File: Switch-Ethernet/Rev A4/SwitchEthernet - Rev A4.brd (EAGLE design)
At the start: 86 x 90 mm, 118 parts, among them J1 22-05-7028-02, J2 DF17(2.0)-20DP-0.5V(57), J3 DF17(4.0)-20DP-0.5V(57), J4 22-05-7058-05, P1 RB1-125BAG1A, T1 H1102FNL, T2 H1102FNL, U1 TC1264-3.3, U2 TC1264-1.8, U3 KSZ8995MA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

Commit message: Route the board
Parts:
- removed LED2, LED3: Green, led:CHIP-LED0603
- removed R1, R2: 1k5, rcl:R0603
- removed TP1, TP3, TP5: TPB1,27, testpad:B1,27
- moved CR1 123.8 mm to (16.5, 61.3), turned to 90 degrees
- moved C19 123.2 mm to (12.4, 60.6), turned to 90 degrees
- moved C20 122.3 mm to (13.0, 48.6), turned to 180 degrees
- moved C21 121.8 mm to (13.0, 46.7), turned to 180 degrees
- moved L3 120.3 mm to (16.5, 54.0), turned to 270 degrees
- moved C18 119.7 mm to (14.0, 60.6), turned to 90 degrees
- moved C4 109.3 mm to (19.7, 60.6), turned to 90 degrees
- moved R27 109.0 mm to (3.17, 58.4), turned to 180 degrees
- moved LED1 107.5 mm to (3.17, 60.3), turned to 90 degrees
- moved C1 106.9 mm to (18.7, 46.4), turned to 270 degrees
- moved U1 101.1 mm to (23.2, 50.2), turned to 90 degrees
- moved U2 101.1 mm to (24.4, 59.1), turned to 90 degrees
- moved C2 96.1 mm to (27.6, 49.8), turned to 90 degrees
- moved C3 94.3 mm to (28.3, 59.1), turned to 90 degrees
- moved C45 54.1 mm to (71.8, 69.5), flipped to the bottom, turned to 270 degrees
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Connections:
- removed net N$2: LED2.A, R1.1
- removed net N$6: LED3.A, R2.1
- net +1V8: no longer R1.2, TP1.TP
- net +3V3: no longer R2.2, TP5.TP
- net +5V: no longer TP3.TP
- net GND: no longer LED2.C, LED3.C
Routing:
- net +3V3: track 19.4 -> 50.1 mm, vias 8 -> 25
- net +1V8: track 0.00 -> 30.1 mm, vias 0 -> 11
- net RST_N: track 2.36 -> 17.6 mm
- net SDA: track 21.7 -> 26.2 mm
- net SCL_EEPROM: track 0.00 -> 3.27 mm
- net SDA_EEPROM: track 0.00 -> 3.14 mm
- net SCL: track 18.2 -> 21.2 mm
- net CT_2: track 49.0 -> 51.1 mm
- net RX1_ISO_N: track 32.4 -> 33.3 mm
- net X1: track 7.57 -> 8.52 mm
- net X2: track 6.21 -> 7.17 mm
- net RX1_ISO_P: track 30.6 -> 31.3 mm
- net TX3_ISO_P: track 56.3 -> 56.9 mm
- net TX3_ISO_N: track 52.4 -> 53.1 mm
- added copper zone on layer 1, net +1V8
- added copper zone on layer 15, net +1V8
- added copper zone on layer 1, net +3V3
- added copper zone on layer 1, net +5V
- added copper zone on layer 1, net PW

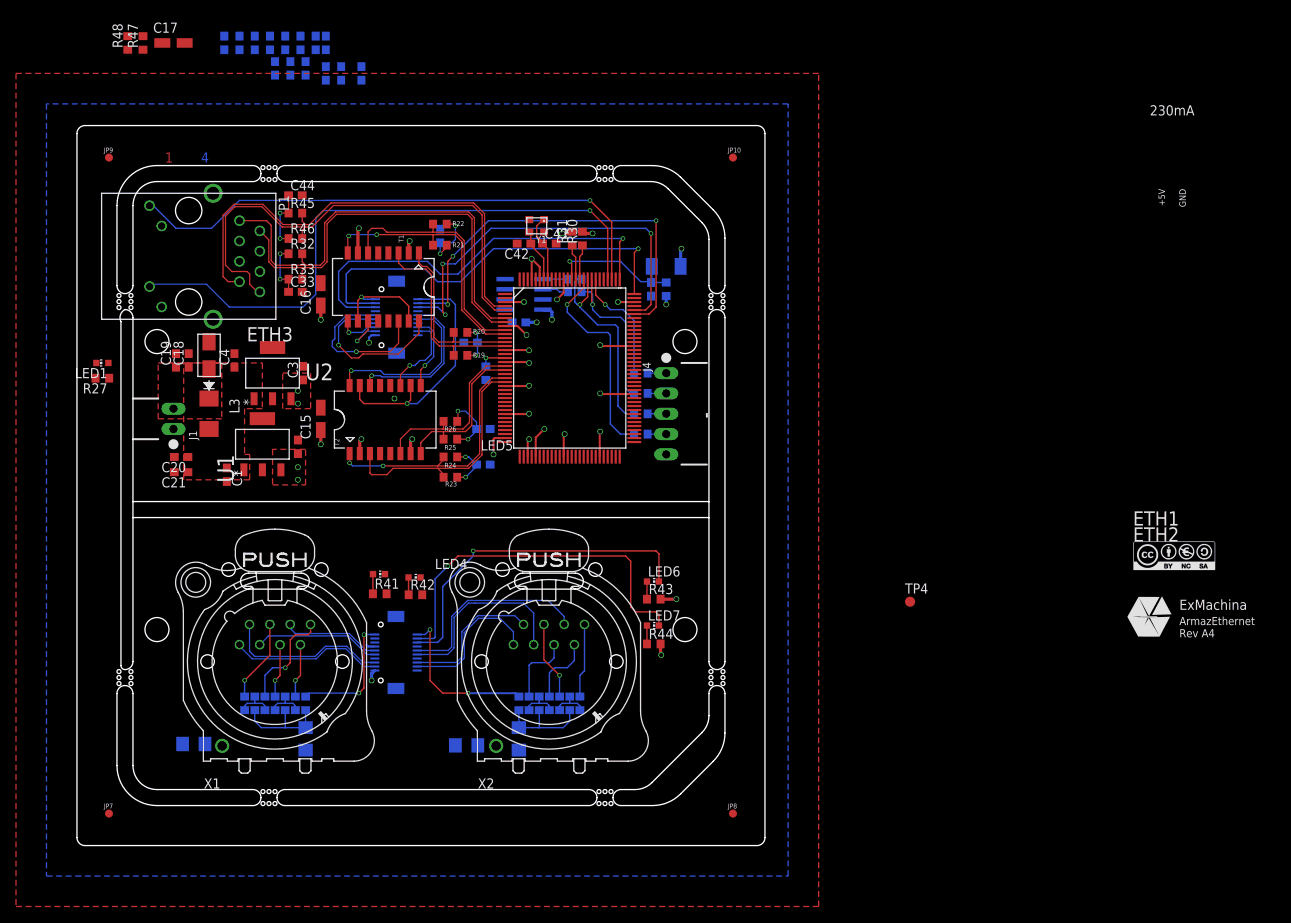
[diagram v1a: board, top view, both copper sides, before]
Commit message: Route LED +5V
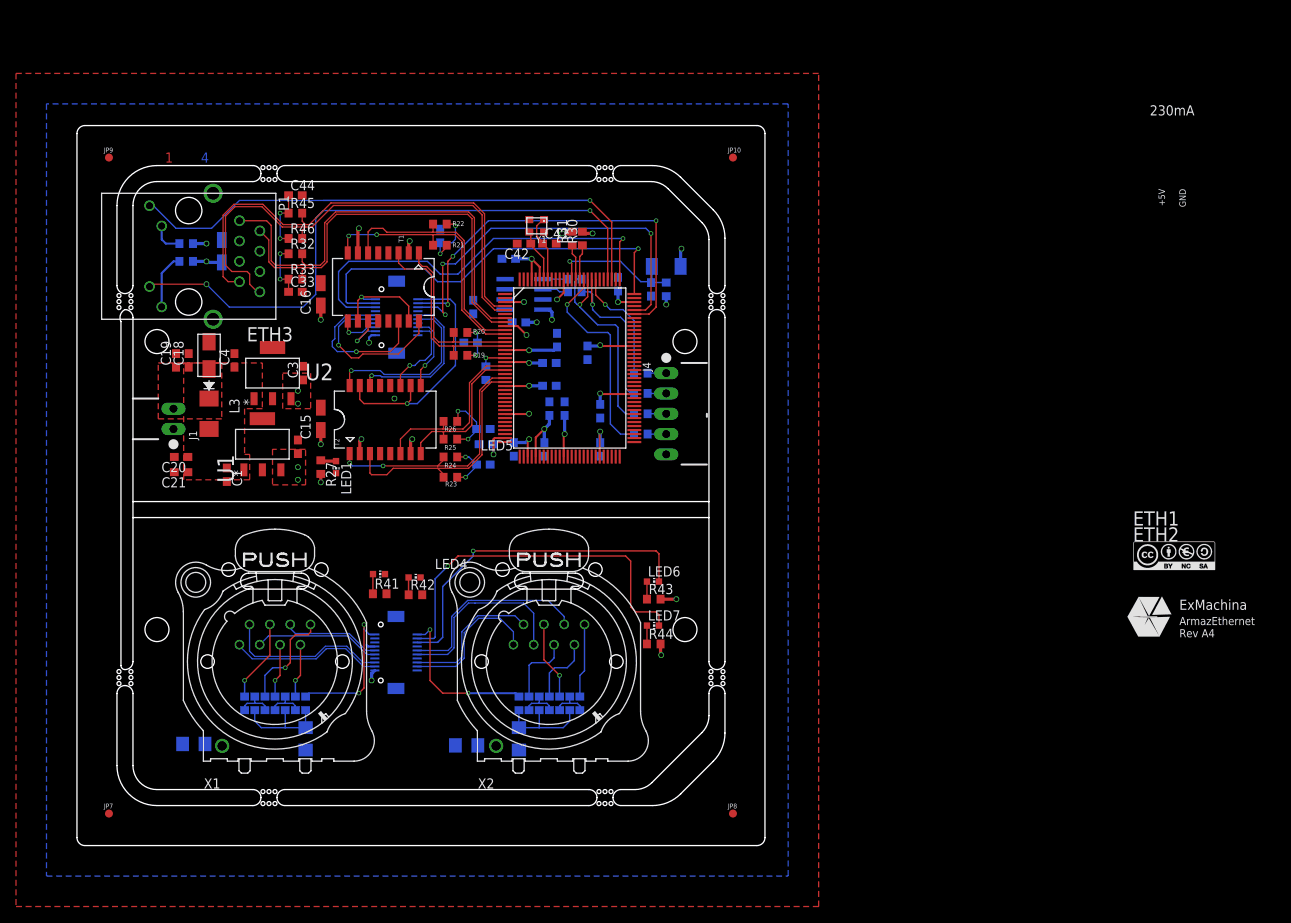
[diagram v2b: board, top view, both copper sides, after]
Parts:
- removed TP4: TPB1,27, testpad:B1,27
- moved C38 62.4 mm to (54.6, 49.5), turned to 270 degrees
- moved C37 60.2 mm to (58.4, 49.5), turned to 270 degrees
- moved C34 58.7 mm to (61.0, 54.6)
- moved C36 58.7 mm to (59.1, 54.6)
- moved C32 55.7 mm to (65.4, 49.5)
- moved C28 53.2 mm to (65.4, 54.3)
- moved C30 53.0 mm to (51.1, 50.2), turned to 0 degrees
- moved C31 50.7 mm to (63.8, 61.6), turned to 270 degrees
- moved C29 50.7 mm to (67.6, 70.2), turned to 90 degrees
- moved C27 48.0 mm to (59.1, 57.5), turned to 180 degrees
- moved C40 47.9 mm to (60.0, 63.2)
- moved C26 47.8 mm to (59.1, 60.3), turned to 180 degrees
- moved C35 43.1 mm to (54.0, 73.3), turned to 0 degrees
- moved C39 39.5 mm to (49.5, 67.3), turned to 270 degrees
- moved LED1 32.0 mm to (32.4, 47.3), turned to 180 degrees
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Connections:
- net GND: no longer TP4.TP
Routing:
- net +1V8: track 30.1 -> 45.5 mm
- net +3V3: track 50.1 -> 64.3 mm, vias 25 -> 28
- net N$35: track 0.00 -> 7.04 mm
- net N$34: track 0.00 -> 4.10 mm
- net CT_1: track 29.1 -> 31.2 mm
- net N$23: track 0.00 -> 1.95 mm
- net +5V: track 0.00 -> 1.05 mm
- net L3-1: vias 1 -> 2

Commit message: Finish the routing
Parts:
- moved LED1 20.7 mm to (11.7, 46.4), turned to 90 degrees
- moved R27 15.3 mm to (15.2, 46.4), turned to 0 degrees
- moved LED5 5.48 mm to (38.0, 30.0), turned to 90 degrees
- moved R41 5.44 mm to (41.5, 35.5)
- moved LED6 2.50 mm to (72.0, 35.5)
- moved LED7 2.50 mm to (72.0, 30.0)
- moved R44 2.50 mm to (72.1, 27.7)
- moved R43 2.50 mm to (72.1, 33.3)
- moved C21 1.59 mm to (14.0, 47.9)
- moved C20 1.59 mm to (14.0, 49.8)
- moved LED4 1.58 mm to (38.0, 35.5), turned to 90 degrees
- moved R42 1.57 mm to (41.5, 30.0)
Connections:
- net GND: no longer J2.11, J2.14, J2.17, J2.4, J2.7, J3.11, J3.14, J3.17, J3.4, J3.7
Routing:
- net L1-1: track 52.4 -> 66.5 mm, vias 1 -> 2
- net L1-2: track 52.2 -> 59.4 mm, vias 1 -> 2
- net +3V3: track 64.3 -> 67.3 mm, vias 28 -> 29
- net L2-2: track 97.7 -> 95.2 mm
- net L2-1: track 92.4 -> 89.9 mm
- net N$36: track 0.00 -> 2.32 mm
- net N$37: track 0.00 -> 2.24 mm
- net GND: track 1.11 -> 0.00 mm
- net +5V: track 1.05 -> 0.00 mm
- net RX1_N: track 25.7 -> 26.4 mm
- net N$20: track 2.47 -> 1.90 mm

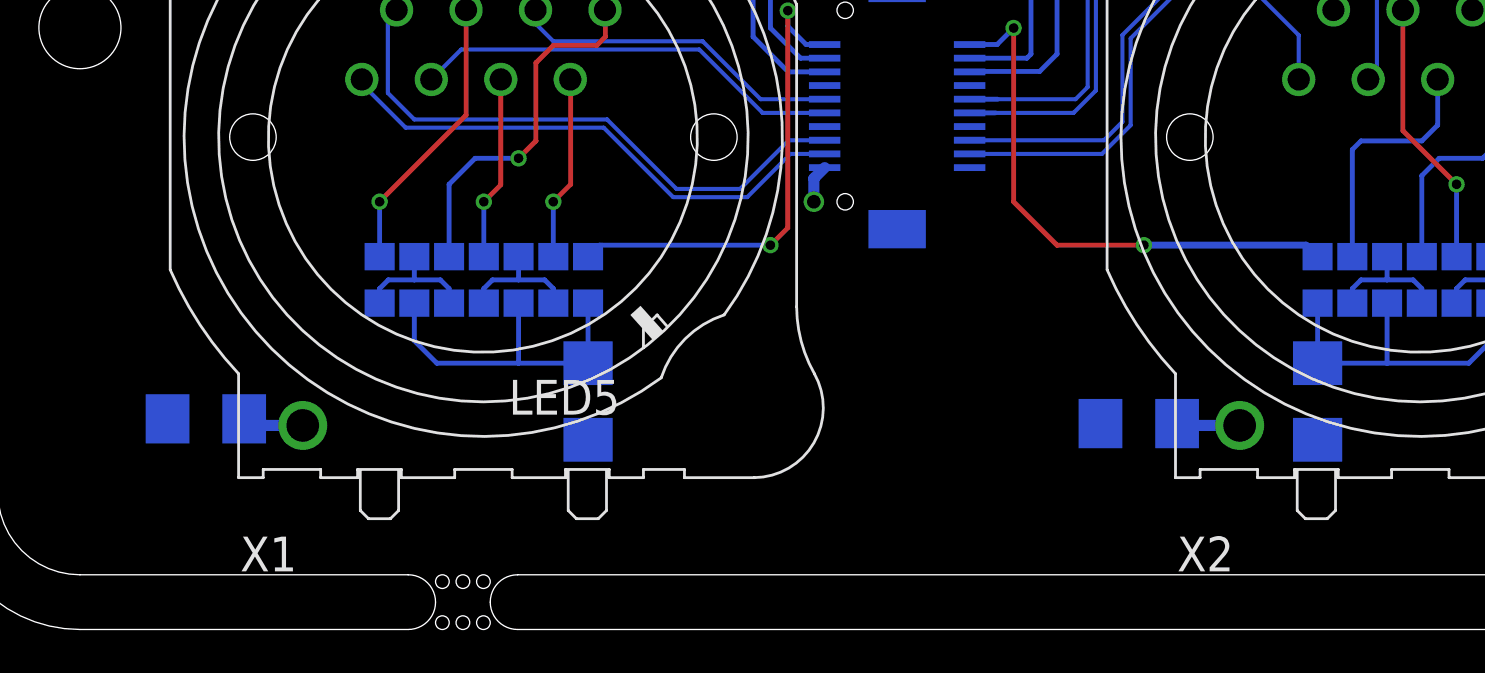
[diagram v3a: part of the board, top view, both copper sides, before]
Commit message: Add bRestrict on the Neutrix panel and route GND nets
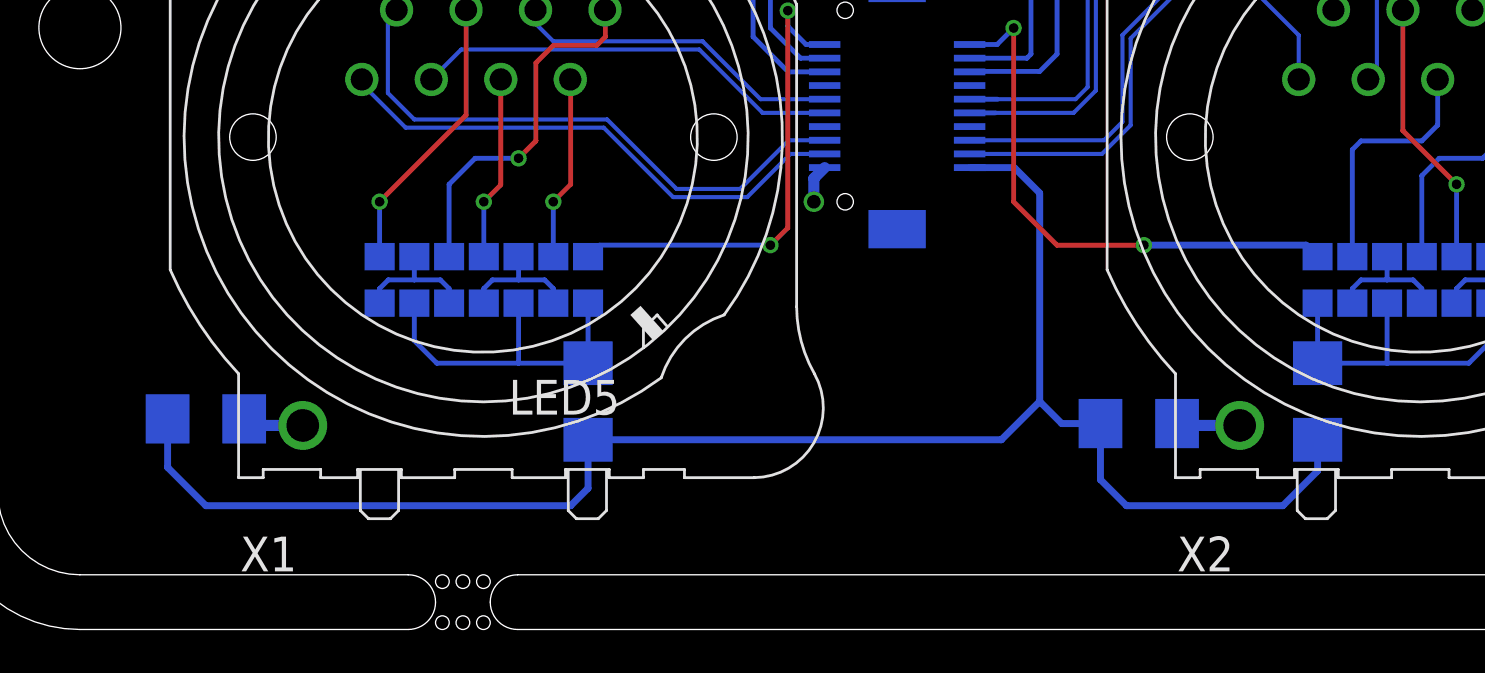
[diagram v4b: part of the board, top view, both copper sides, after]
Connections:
- net GND: now also J2.11, J3.11
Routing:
- net GND: track 0.00 -> 62.0 mm
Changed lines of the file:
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@@
 <layers>
 <layer number="1" name="Top" color="16" fill="1" visible="yes" active="yes"/>
-<layer number="2" name="Route2" color="17" fill="1" visible="yes" active="yes"/>
+<layer number="2" name="Route2" color="17" fill="1" visible="no" active="yes"/>
 <layer number="14" name="Route14" color="1" fill="6" visible="no" active="no"/>
-<layer number="15" name="Route15" color="19" fill="1" visible="yes" active="yes"/>
+<layer number="15" name="Route15" color="19" fill="1" visible="no" active="yes"/>
 <layer number="16" name="Bottom" color="21" fill="1" visible="yes" active="yes"/>
 <layer number="17" name="Pads" color="18" fill="1" visible="yes" active="yes"/>
@@
 <layer number="39" name="tKeepout" color="4" fill="11" visible="no" active="yes"/>
 <layer number="40" name="bKeepout" color="3" fill="11" visible="no" active="yes"/>
-<layer number="41" name="tRestrict" color="4" fill="10" visible="yes" active="yes"/>
+<layer number="41" name="tRestrict" color="4" fill="10" visible="no" active="yes"/>
 <layer number="42" name="bRestrict" color="3" fill="10" visible="no" active="yes"/>
 <layer number="43" name="vRestrict" color="2" fill="10" visible="no" active="yes"/>
@@
 <dimension x1="64" y1="7" x2="72" y2="30" x3="99.5" y3="18.5" textsize="1.778" layer="48" dtype="vertical"/>
 <dimension x1="72" y1="30" x2="72" y2="35.5" x3="99.5" y3="32.75" textsize="1.778" layer="48" dtype="vertical"/>
+<polygon width="0.4064" layer="42">
+<vertex x="3.81" y="41.91"/>
+<vertex x="83.82" y="41.91"/>
+<vertex x="83.82" y="9.525"/>
+<vertex x="83.82" y="2.54"/>
+<vertex x="19.05" y="2.54"/>
+<vertex x="3.81" y="2.54"/>
+</polygon>
 </plain>
 <attributes>
@@
 <via x="39.6875" y="55.88" extent="1-16" drill="0.5"/>
 <contactref element="J4" pad="5"/>
-<wire x1="13.205" y1="12.7" x2="18.7325" y2="45.505" width="0" layer="19" extent="1-16"/>
+<contactref element="J2" pad="11"/>
+<contactref element="J3" pad="11"/>
+<wire x1="42.525" y1="21.885" x2="44.155" y2="21.885" width="0.254" layer="16"/>
+<wire x1="44.155" y1="21.885" x2="45.085" y2="20.955" width="0.254" layer="16"/>
+<wire x1="45.085" y1="20.955" x2="45.085" y2="13.335" width="0.254" layer="16"/>
+<wire x1="45.085" y1="13.335" x2="45.8925" y2="12.5275" width="0.254" layer="16"/>
+<wire x1="45.8925" y1="12.5275" x2="47.3075" y2="12.5275" width="0.254" layer="16"/>
+<wire x1="55.245" y1="11.935" x2="55.245" y2="10.795" width="0.254" layer="16"/>
+<wire x1="55.245" y1="10.795" x2="53.975" y2="9.525" width="0.254" layer="16"/>
+<wire x1="53.975" y1="9.525" x2="48.26" y2="9.525" width="0.254" layer="16"/>
+<wire x1="48.26" y1="9.525" x2="47.3075" y2="10.4775" width="0.254" layer="16"/>
+<wire x1="47.3075" y1="10.4775" x2="47.3075" y2="12.5275" width="0.254" layer="16"/>
+<wire x1="13.205" y1="12.7" x2="13.205" y2="10.925" width="0.254" layer="16"/>
+<wire x1="13.205" y1="10.925" x2="14.605" y2="9.525" width="0.254" layer="16"/>
+<wire x1="14.605" y1="9.525" x2="27.94" y2="9.525" width="0.254" layer="16"/>
+<wire x1="27.94" y1="9.525" x2="28.575" y2="10.16" width="0.254" layer="16"/>
+<wire x1="28.575" y1="10.16" x2="28.575" y2="11.935" width="0.254" layer="16"/>
+<wire x1="28.575" y1="11.935" x2="43.685" y2="11.935" width="0.254" layer="16"/>
+<wire x1="43.685" y1="11.935" x2="45.085" y2="13.335" width="0.254" layer="16"/>
+<wire x1="51.65" y1="47.625" x2="44.155" y2="21.885" width="0" layer="19" extent="16-16"/>
+<wire x1="42.615" y1="63.795" x2="48.3625" y2="62.865" width="0" layer="19" extent="16-16"/>
 </signal>
 <signal name="L3-1">

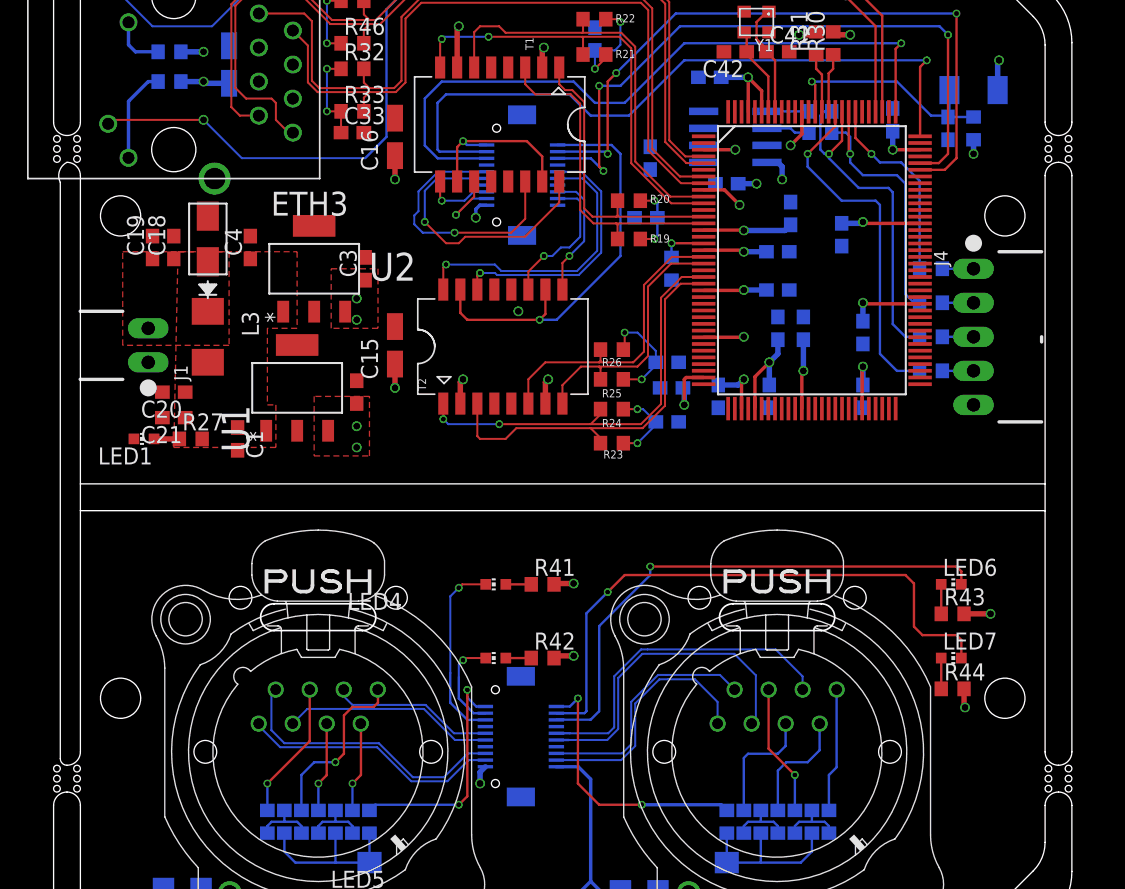
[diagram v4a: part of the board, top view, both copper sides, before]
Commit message: Adjust connector possition and panelize the board
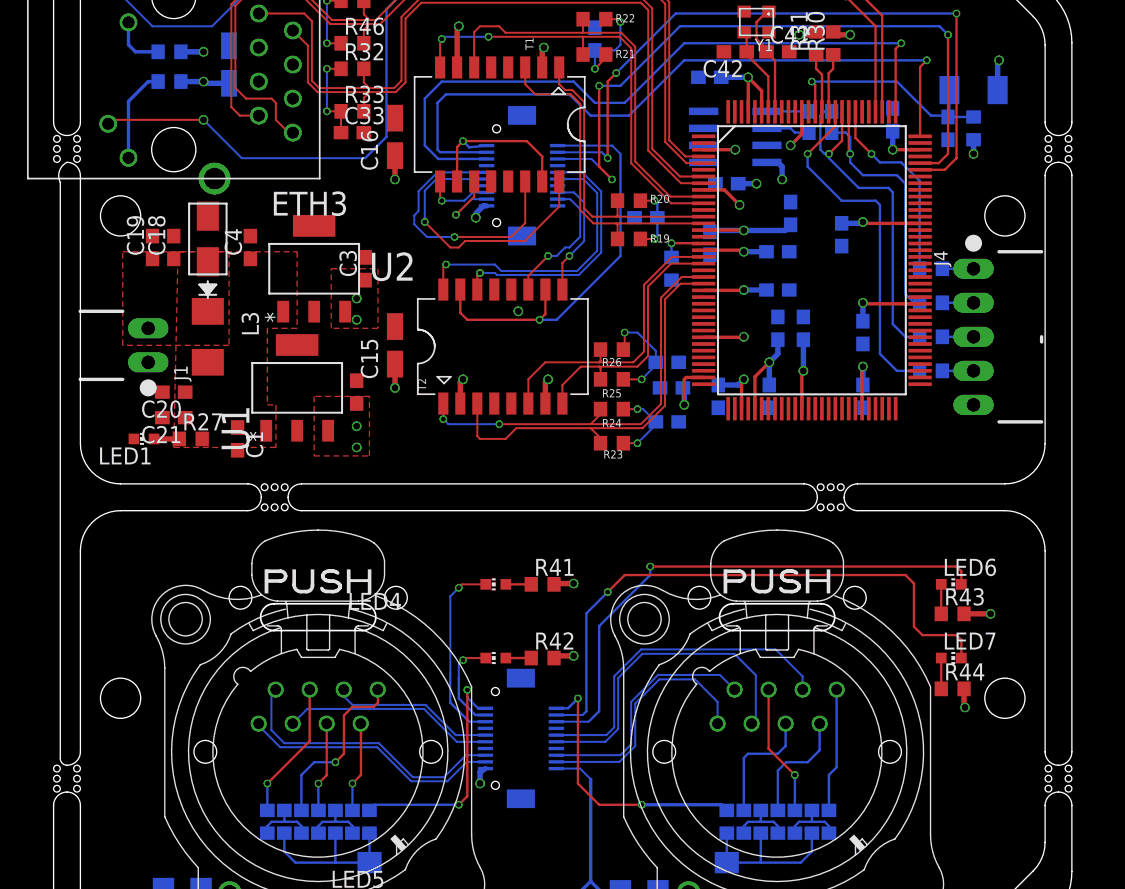
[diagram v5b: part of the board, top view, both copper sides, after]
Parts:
- moved C39 7.75 mm to (54.0, 61.0)
- moved J2 0.14 mm to (39.9, 24.0)
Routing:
- net +1V8: track 45.5 -> 48.1 mm
- net L2-1: track 89.9 -> 91.7 mm
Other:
- outline, holes or cut-outs redrawn
